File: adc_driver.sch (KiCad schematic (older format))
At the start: 20 parts, among them U17 DG412xUE, U18 AD8421ARZ, U19 ADA4932-1YCPZ-R7

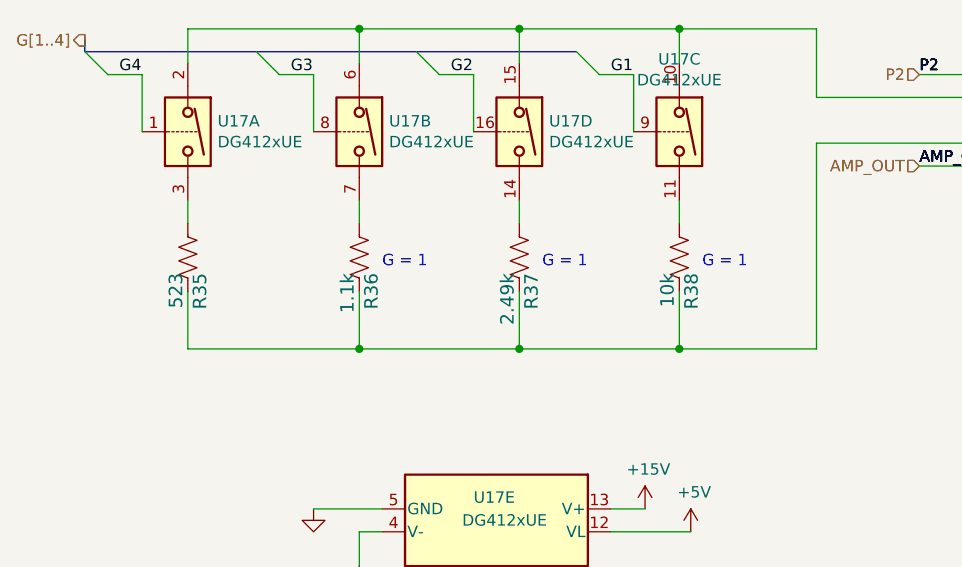
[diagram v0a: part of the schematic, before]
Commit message: offset adjust to feedback buffer
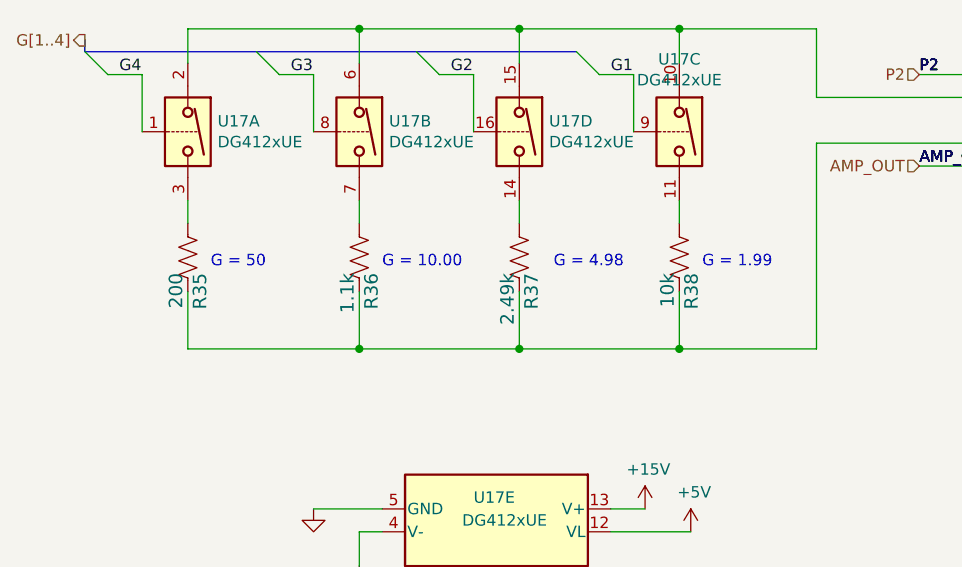
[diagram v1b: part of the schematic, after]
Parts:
- R35: value 523 -> 200; Manf# RC0603FR-07523RL -> RC0603FR-07200RL
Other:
- note added: "G = 1.99"
- note added: "G = 10.00"
- note added: "G = 4.98"
- note added: "G = 50"
- note removed: "G = 1"
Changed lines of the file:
@@
 $Descr A4 11693 8268
 encoding utf-8
-Sheet 4 5
+Sheet 4 6
 Title ""
 Date ""
@@
 AR Path="/6032F251/608FDC40/60A6A83E" Ref="R35"  Part="1"
 F 0 "R35" V 1297 4418 59  0000 L CNN
-F 1 "523" V 1402 4418 59  0000 L CNN
+F 1 "200" V 1402 4418 59  0000 L CNN
 F 2 "Resistor_SMD:R_0603_1608Metric" H 1350 4350 50  0001 C CNN
 F 3 "" H 1350 4350 50  0001 C CNN
-F 4 "RC0603FR-07523RL" H 1297 4518 50  0001 C CNN "Manf#"
+F 4 "RC0603FR-07200RL" H 1297 4518 50  0001 C CNN "Manf#"
 F 5 "1%" H 1350 4350 50  0001 C CNN "Tolerance"
 	1    1350 4350
@@
 Text Notes 5250 3450 0    50   ~ 0
 InAmp
-Text Notes 2900 4400 0    50   ~ 0
-G = 1
 Text Label 4550 3950 0    50   ~ 0
 AMP_OUT
@@
 Text Notes 5250 3450 0    50   ~ 0
 InAmp
-Text Notes 2200 4400 0    50   ~ 0
-G = 1
 Text Label 4550 3950 0    50   ~ 0
 AMP_OUT
@@
 InAmp
 Text Notes 3600 4400 0    50   ~ 0
-G = 1
+G = 1.99
 Text Label 9500 4150 0    50   ~ 0
 VCM
@@
 Wire Wire Line
 	7700 4850 7700 4750
+Connection ~ 7700 4850
+Connection ~ 7700 4750
+Wire Wire Line
+	7700 4750 7700 4650
 Wire Bus Line
 	900  3450 3050 3450
-Connection ~ 7700 4850
-Connection ~ 7700 4750
-Wire Wire Line
-	7700 4750 7700 4650
+Text Notes 2950 4400 0    50   ~ 0
+G = 4.98
+Text Notes 2200 4400 0    50   ~ 0
+G = 10.00
+Text Notes 1450 4400 0    50   ~ 0
+G = 50
 $EndSCHEMATC

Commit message: updates to pcb layout
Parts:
- U18: footprint (none) -> digikey-footprints:TSSOP-8_W3mm
- U19: footprint CP_16_2_ADI -> digikey-footprints:VFQFN-16-1EP_3x3mm
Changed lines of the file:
@@
 F 0 "U19" H 8500 4287 60  0000 C CNN
 F 1 "ADA4932-1YCPZ-R7" H 8500 4181 60  0000 C CNN
-F 2 "CP_16_2_ADI" H 8500 4140 60  0001 C CNN
+F 2 "digikey-footprints:VFQFN-16-1EP_3x3mm" H 8500 4140 60  0001 C CNN
 F 3 "" H 7700 3800 60  0000 C CNN
 F 4 "ADA4932-1YCPZ-R7" H 7700 3800 50  0001 C CNN "Manf#"
@@
 F 0 "U18" H 5694 3796 50  0000 L CNN
 F 1 "AD8421ARZ" H 5694 3705 50  0000 L CNN
-F 2 "" H 5050 3750 50  0001 C CNN
+F 2 "digikey-footprints:TSSOP-8_W3mm" H 5050 3750 50  0001 C CNN
 F 3 "https://www.analog.com/media/en/technical-documentation/data-sheets/AD8421.pdf" H 5600 3350 50  0001 C CNN
 F 4 "AD8421ARMZ" H 5694 3896 50  0001 C CNN "Manf#"

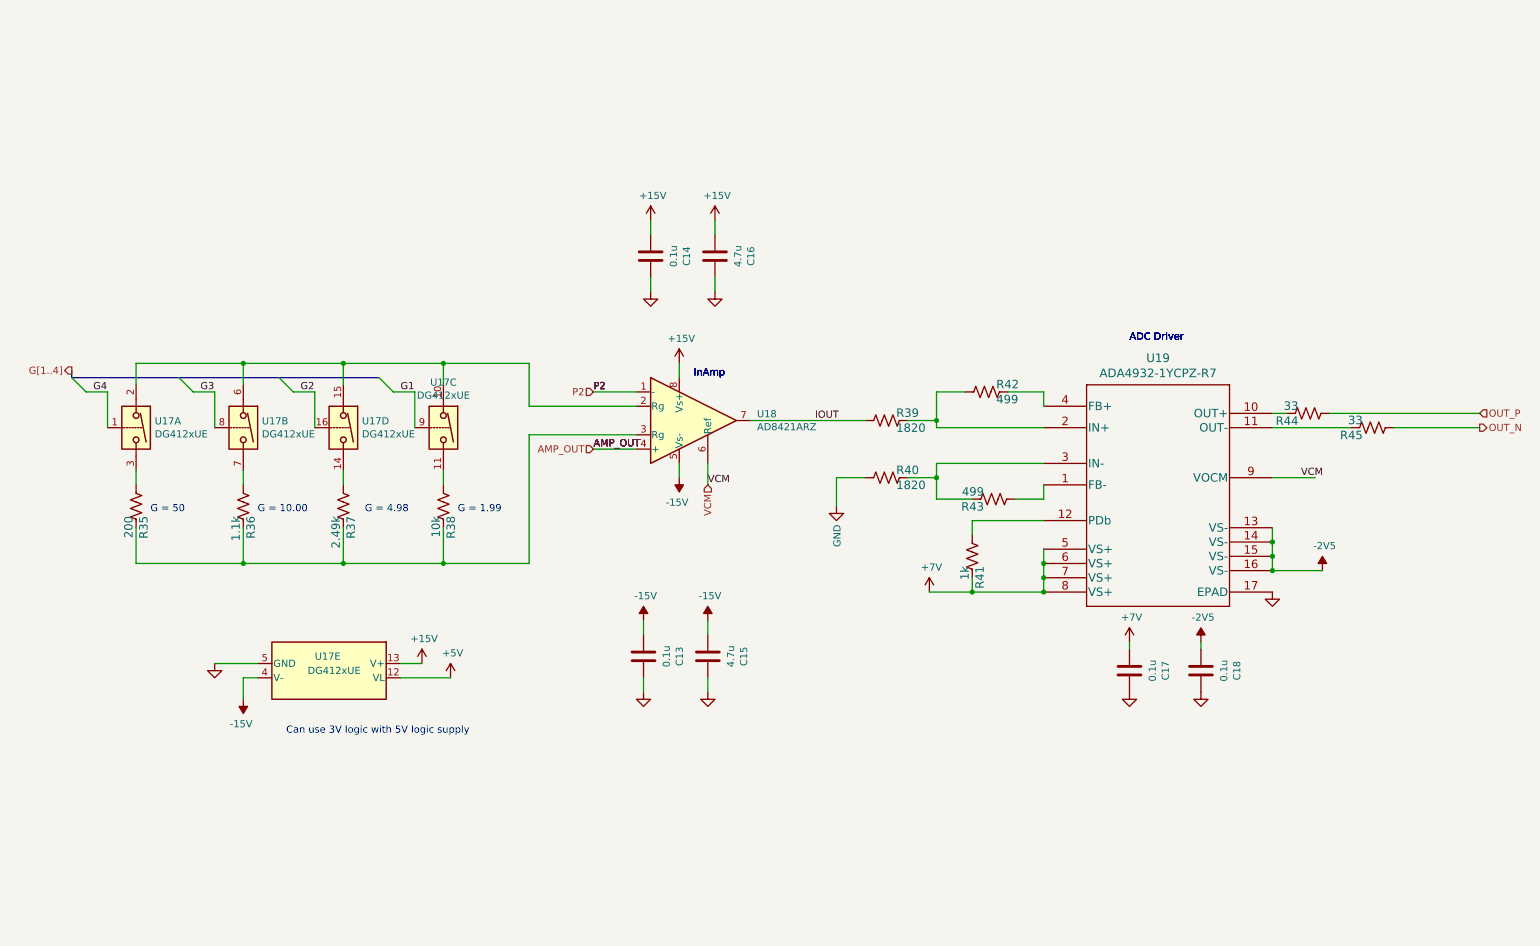
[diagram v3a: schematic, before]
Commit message: added switching (partially) for current clamp
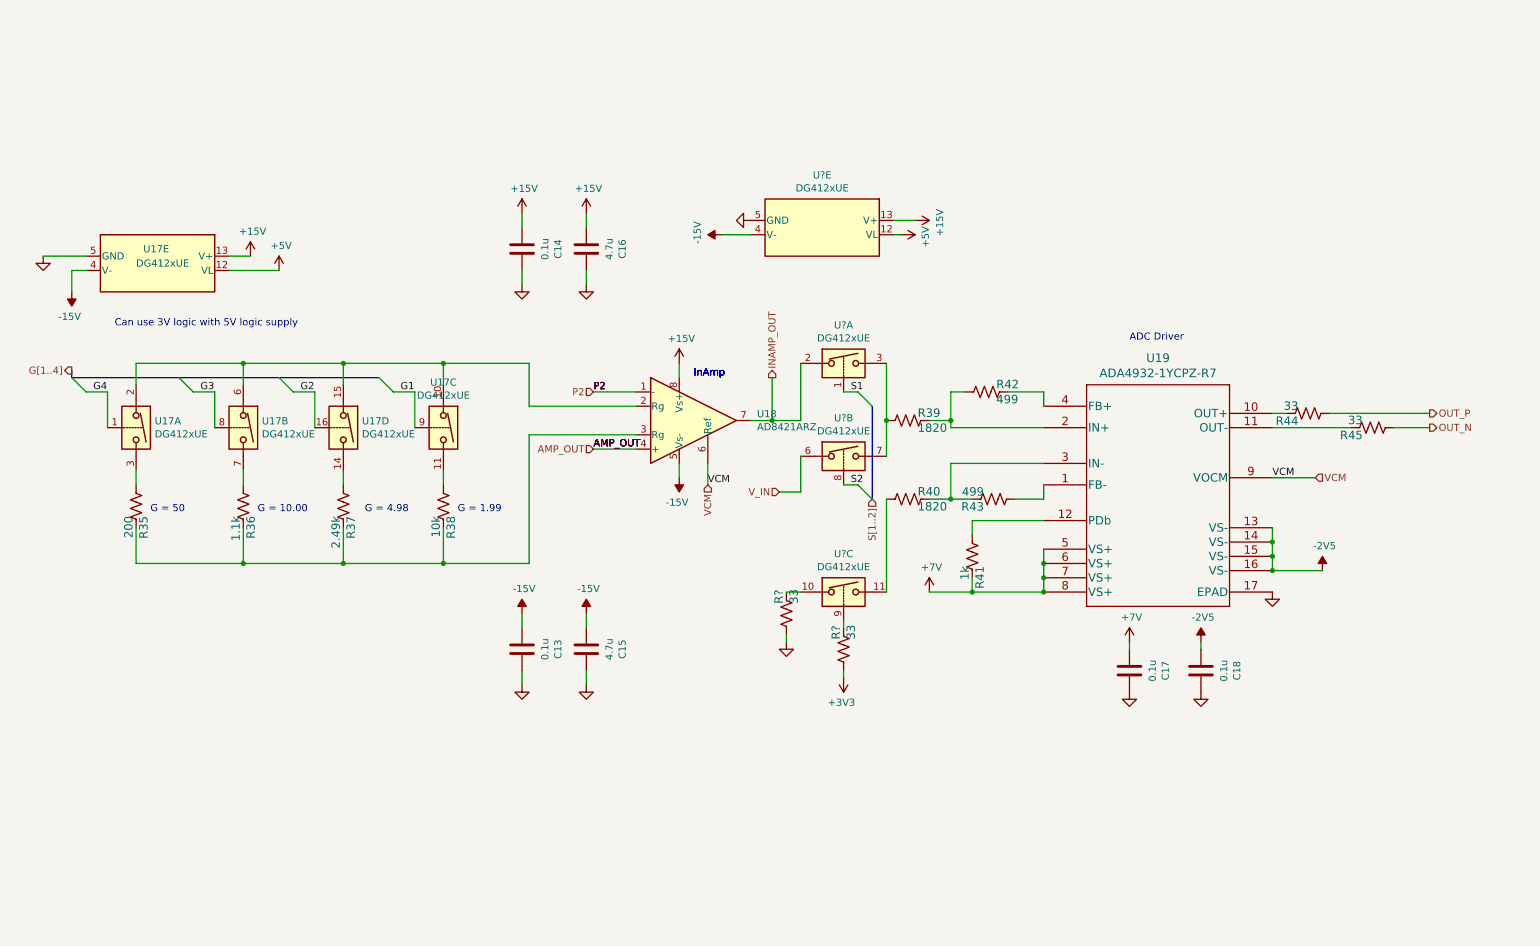
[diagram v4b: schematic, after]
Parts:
- added R? (x2): 33, Resistor_SMD:R_0603_1608Metric, symbol Device:R_US
- added U? (x4): DG412xUE, Package_SO:TSSOP-16_4.4x5mm_P0.65mm, symbol Analog_Switch:DG412xUE
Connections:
- net +15V: now also U?.13 (V+)
- net +5V: now also U?.12 (VL)
- net -15V: now also U?.4 (V-)
- net GND: now also R?.2, U?.5 (GND); no longer R40.2
- net IOUT: no longer names the net of R39.2
- net IOUT: now also U?.3, U?.7; no longer U18.7
- new net: R40.2, U?.11
- new net: R?.1, U?.10
- new net: R?.1, U?.9
- new net +3V3: R?.2
- new net INAMP_OUT: U18.7, U?.2
- new net S1: U?.1
- new net S2: U?.8
- new net V_IN: U?.6
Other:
- note added: "ADC Driver \nAlternative part LMP8350"
- note removed: "ADC Driver"
- moved on the sheet: C13, C14, C15, C16, R39, R40, U17E

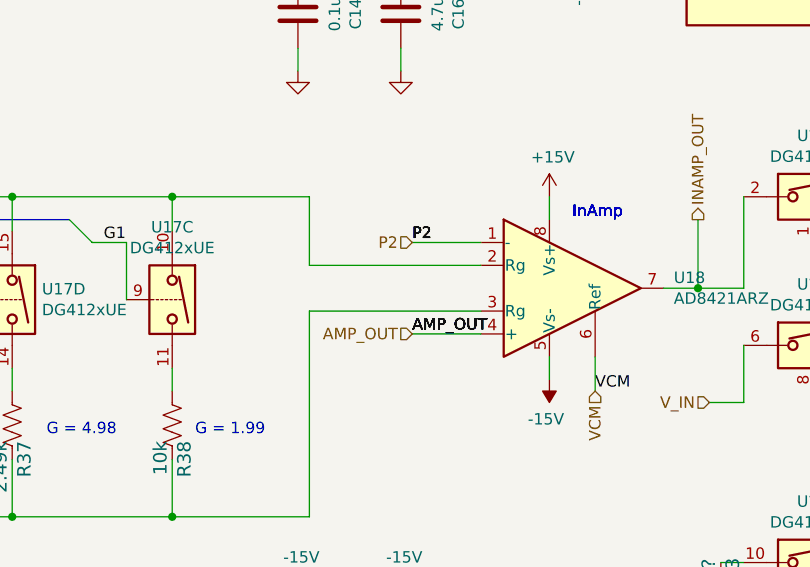
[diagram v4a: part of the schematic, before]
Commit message: before adding Howland for current clamp
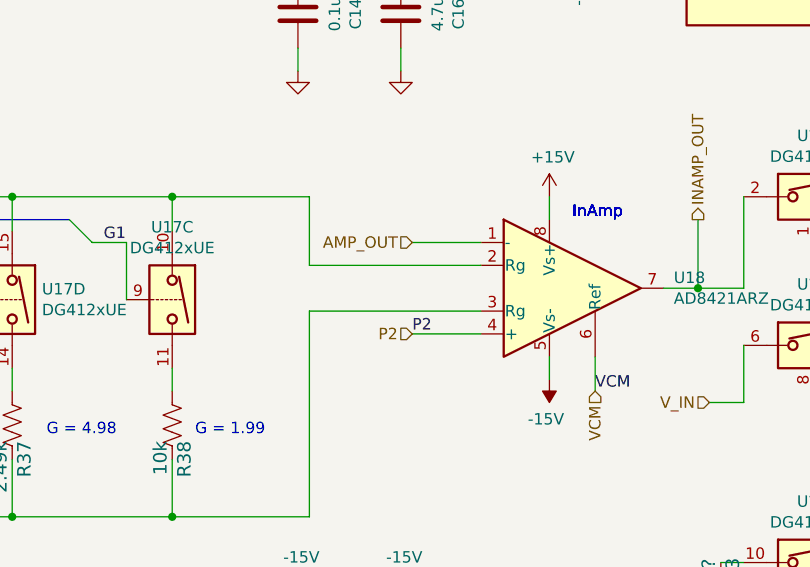
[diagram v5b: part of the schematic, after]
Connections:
- net AMP_OUT: now also U18.1 (-); no longer U18.4 (+)
- net P2: now also U18.4 (+); no longer U18.1 (-)
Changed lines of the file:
@@
 $Descr A4 11693 8268
 encoding utf-8
-Sheet 3 6
+Sheet 6 6
 Title ""
 Date ""
@@
 	1    0    0    -1
 $EndComp
+Text Notes 5250 3450 0    50   ~ 0
+InAmp
 Text Label 4550 3950 0    50   ~ 0
-AMP_OUT
-Text Label 4550 3550 0    50   ~ 0
 P2
 Text Notes 5250 3450 0    50   ~ 0
 InAmp
-Text Label 4550 3950 0    50   ~ 0
-AMP_OUT
-Text Label 4550 3550 0    50   ~ 0
-P2
-Text Notes 5250 3450 0    50   ~ 0
-InAmp
-Text Label 4550 3950 0    50   ~ 0
-AMP_OUT
-Text Label 4550 3550 0    50   ~ 0
-P2
 Text Notes 5250 3450 0    50   ~ 0
 InAmp
 Text Label 5350 4200 0    50   ~ 0
 VCM
-Text Label 4550 3950 0    50   ~ 0
-AMP_OUT
-Text Label 4550 3550 0    50   ~ 0
-P2
 Text Notes 5250 3450 0    50   ~ 0
 InAmp
@@
 Text Notes 8300 3200 0    50   ~ 0
 ADC Driver \nAlternative part LMP8350
+Text HLabel 4550 3950 0    50   Input ~ 0
+P2
 Text HLabel 4550 3550 0    50   Input ~ 0
-P2
-Text HLabel 4550 3950 0    50   Input ~ 0
 AMP_OUT
 Text HLabel 5350 4200 3    50   Input ~ 0

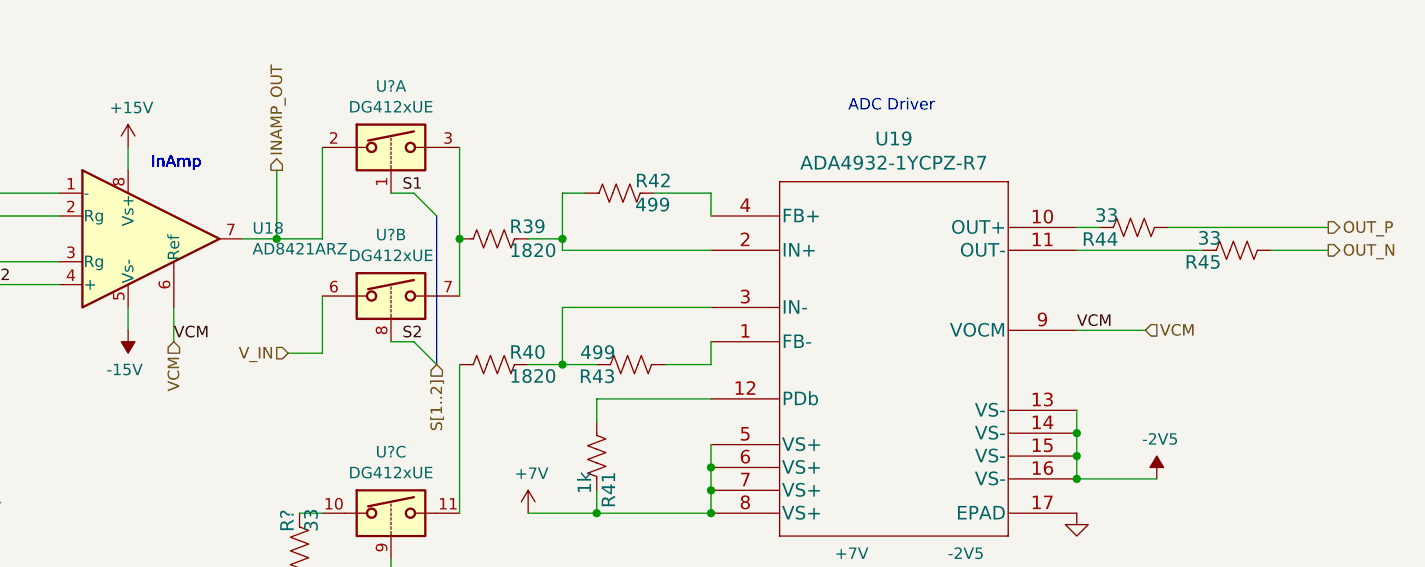
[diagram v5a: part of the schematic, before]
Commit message: updates to README
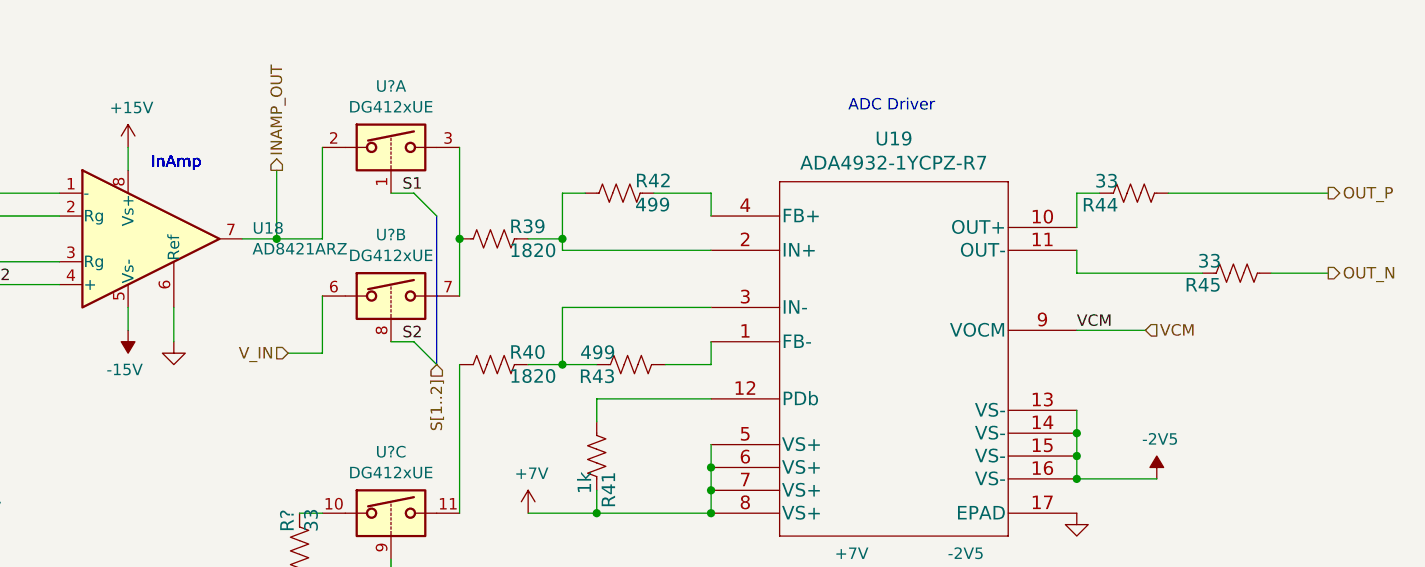
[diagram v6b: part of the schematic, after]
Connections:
- net GND: now also U18.6 (Ref)
- net VCM: no longer U18.6 (Ref)
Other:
- moved on the sheet: R44, R45
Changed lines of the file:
@@
 Text Notes 5250 3450 0    50   ~ 0
 InAmp
-Text Label 5350 4200 0    50   ~ 0
-VCM
 Text Notes 5250 3450 0    50   ~ 0
 InAmp
@@
 Text HLabel 4550 3550 0    50   Input ~ 0
 AMP_OUT
-Text HLabel 5350 4200 3    50   Input ~ 0
-VCM
-Text HLabel 10400 3700 2    50   Output ~ 0
+Text HLabel 10400 3550 2    50   Output ~ 0
 OUT_P
-Text HLabel 10400 3800 2    50   Output ~ 0
+Text HLabel 10400 3900 2    50   Output ~ 0
 OUT_N
 Text Label 3200 3550 0    50   ~ 0
@@
 	6900 4300 7050 4300
 Wire Wire Line
-	9300 3700 9400 3700
+	9300 3550 9400 3550
 Wire Wire Line
 	9300 4150 9600 4150
@@
 L Device:R_US R?
 U 1 1 60C9B5A9
-P 9550 3700
+P 9550 3550
 AR Path="/6032F251/60C9B5A9" Ref="R?"  Part="1"
 AR Path="/6032F251/608FDC40/60C9B5A9" Ref="R44"  Part="1"
-F 0 "R44" V 9497 3768 59  0000 L CNN
-F 1 "33" V 9602 3768 59  0000 L CNN
-F 2 "Resistor_SMD:R_0603_1608Metric" H 9550 3700 50  0001 C CNN
-F 3 "" H 9550 3700 50  0001 C CNN
-F 4 "RC0603FR-0733RL" H 9497 3868 50  0001 C CNN "Manf#"
-F 5 "1%" H 9550 3700 50  0001 C CNN "Tolerance"
-	1    9550 3700
+F 0 "R44" V 9497 3618 59  0000 L CNN
+F 1 "33" V 9602 3618 59  0000 L CNN
+F 2 "Resistor_SMD:R_0603_1608Metric" H 9550 3550 50  0001 C CNN
+F 3 "" H 9550 3550 50  0001 C CNN
+F 4 "RC0603FR-0733RL" H 9497 3718 50  0001 C CNN "Manf#"
+F 5 "1%" H 9550 3550 50  0001 C CNN "Tolerance"
+	1    9550 3550
 	0    -1   -1   0
 $EndComp
 Wire Wire Line
-	9700 3700 10400 3700
+	9700 3550 10400 3550
 $Comp
 L Device:R_US R?
 U 1 1 60CA6FC0
-P 10000 3800
+P 10000 3900
 AR Path="/6032F251/60CA6FC0" Ref="R?"  Part="1"
 AR Path="/6032F251/608FDC40/60CA6FC0" Ref="R45"  Part="1"
-F 0 "R45" V 9947 3868 59  0000 L CNN
-F 1 "33" V 10052 3868 59  0000 L CNN
-F 2 "Resistor_SMD:R_0603_1608Metric" H 10000 3800 50  0001 C CNN
-F 3 "" H 10000 3800 50  0001 C CNN
-F 4 "RC0603FR-0733RL" H 9947 3968 50  0001 C CNN "Manf#"
-F 5 "1%" H 10000 3800 50  0001 C CNN "Tolerance"
-	1    10000 3800
+F 0 "R45" V 9947 3968 59  0000 L CNN
+F 1 "33" V 10052 3968 59  0000 L CNN
+F 2 "Resistor_SMD:R_0603_1608Metric" H 10000 3900 50  0001 C CNN
+F 3 "" H 10000 3900 50  0001 C CNN
+F 4 "RC0603FR-0733RL" H 9947 4068 50  0001 C CNN "Manf#"
+F 5 "1%" H 10000 3900 50  0001 C CNN "Tolerance"
+	1    10000 3900
 	0    -1   -1   0
 $EndComp
 Wire Wire Line
-	9300 3800 9850 3800
-Wire Wire Line
-	10150 3800 10400 3800
+	9300 3900 9850 3900
+Wire Wire Line
+	10150 3900 10400 3900
 Wire Wire Line
 	9300 4700 9300 4600
@@
 Wire Wire Line
 	6300 5200 6300 5150
+$Comp
+L power:GND #PWR?
+U 1 1 60A8B45A
+P 5350 4200
+AR Path="/6032F251/60A8B45A" Ref="#PWR?"  Part="1"
+AR Path="/6032F251/608FDC40/60A8B45A" Ref="#PWR?"  Part="1"
+F 0 "#PWR?" H 5350 3950 50  0001 C CNN
+F 1 "GND" V 5355 4072 50  0001 R CNN
+F 2 "" H 5350 4200 50  0001 C CNN
+F 3 "" H 5350 4200 50  0001 C CNN
+	1    5350 4200
+	1    0    0    -1
+$EndComp
+Wire Wire Line
+	9300 3700 9300 3550
+Wire Wire Line
+	9300 3800 9300 3900
 Wire Bus Line
 	900  3450 3050 3450
